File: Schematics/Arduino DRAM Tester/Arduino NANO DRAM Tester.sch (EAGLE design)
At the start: 53 parts, among them IC1 4164/41256, IC2 4116, Q1 2N3906

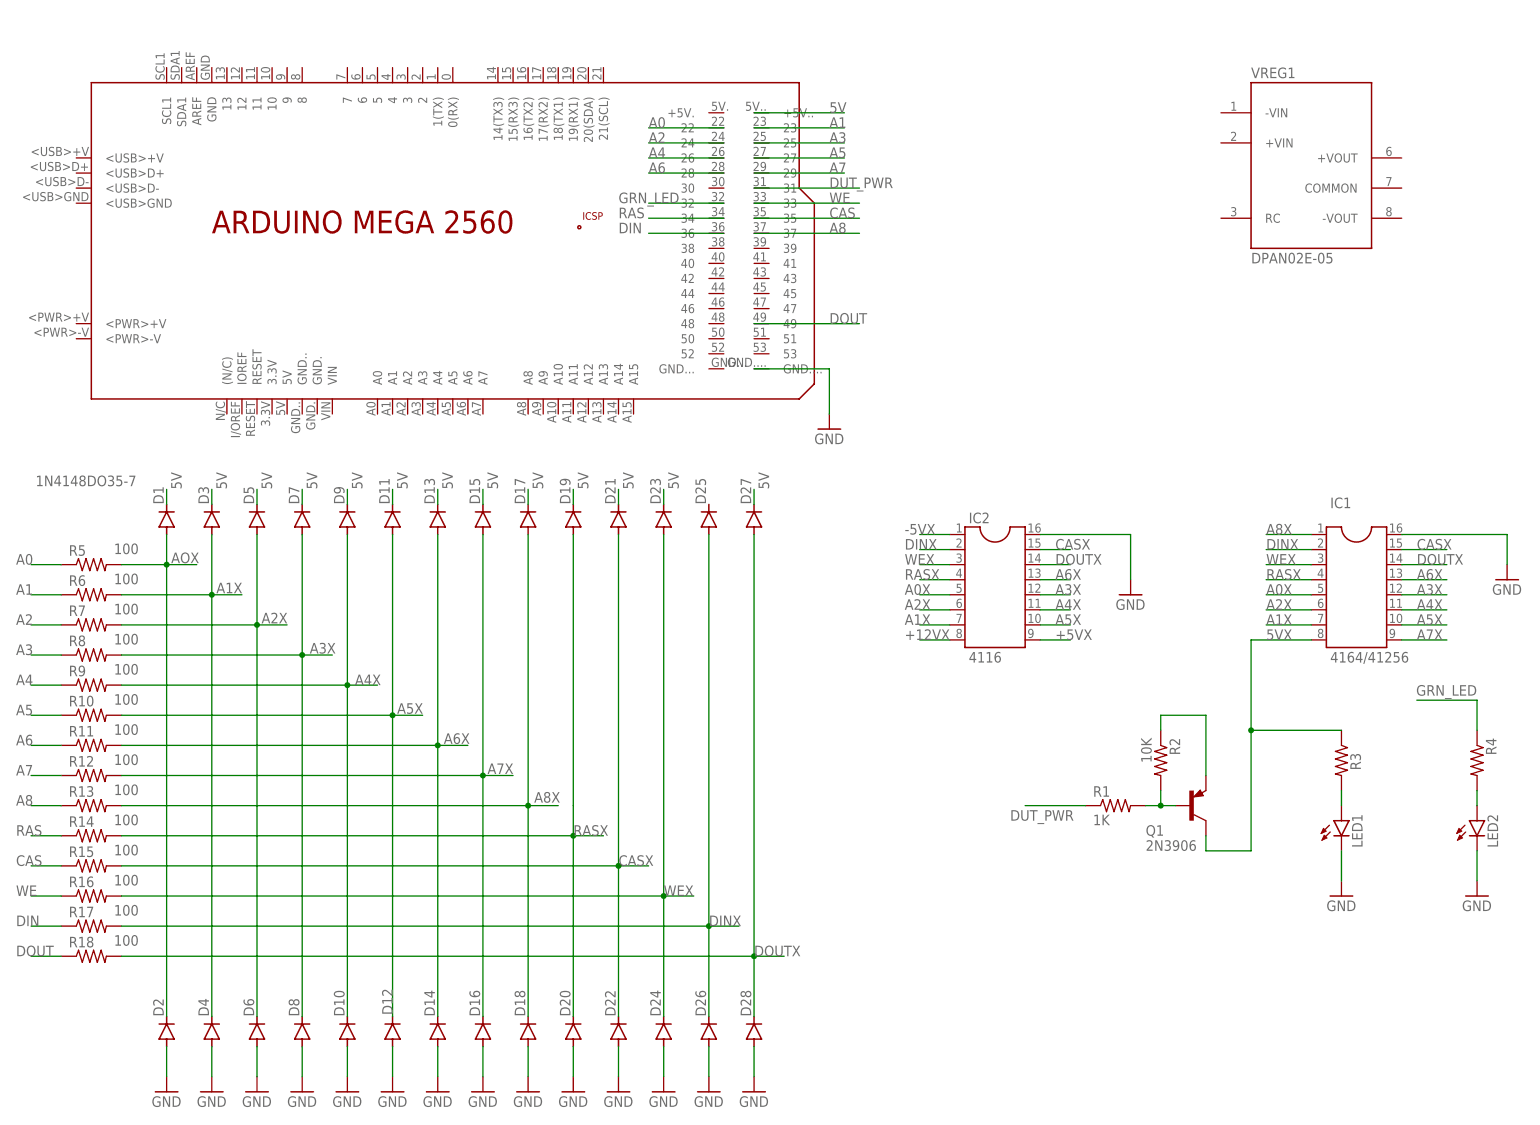
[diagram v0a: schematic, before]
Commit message: Added  def for Nano and Micro. Tested on Mega and Micro. Will add display next
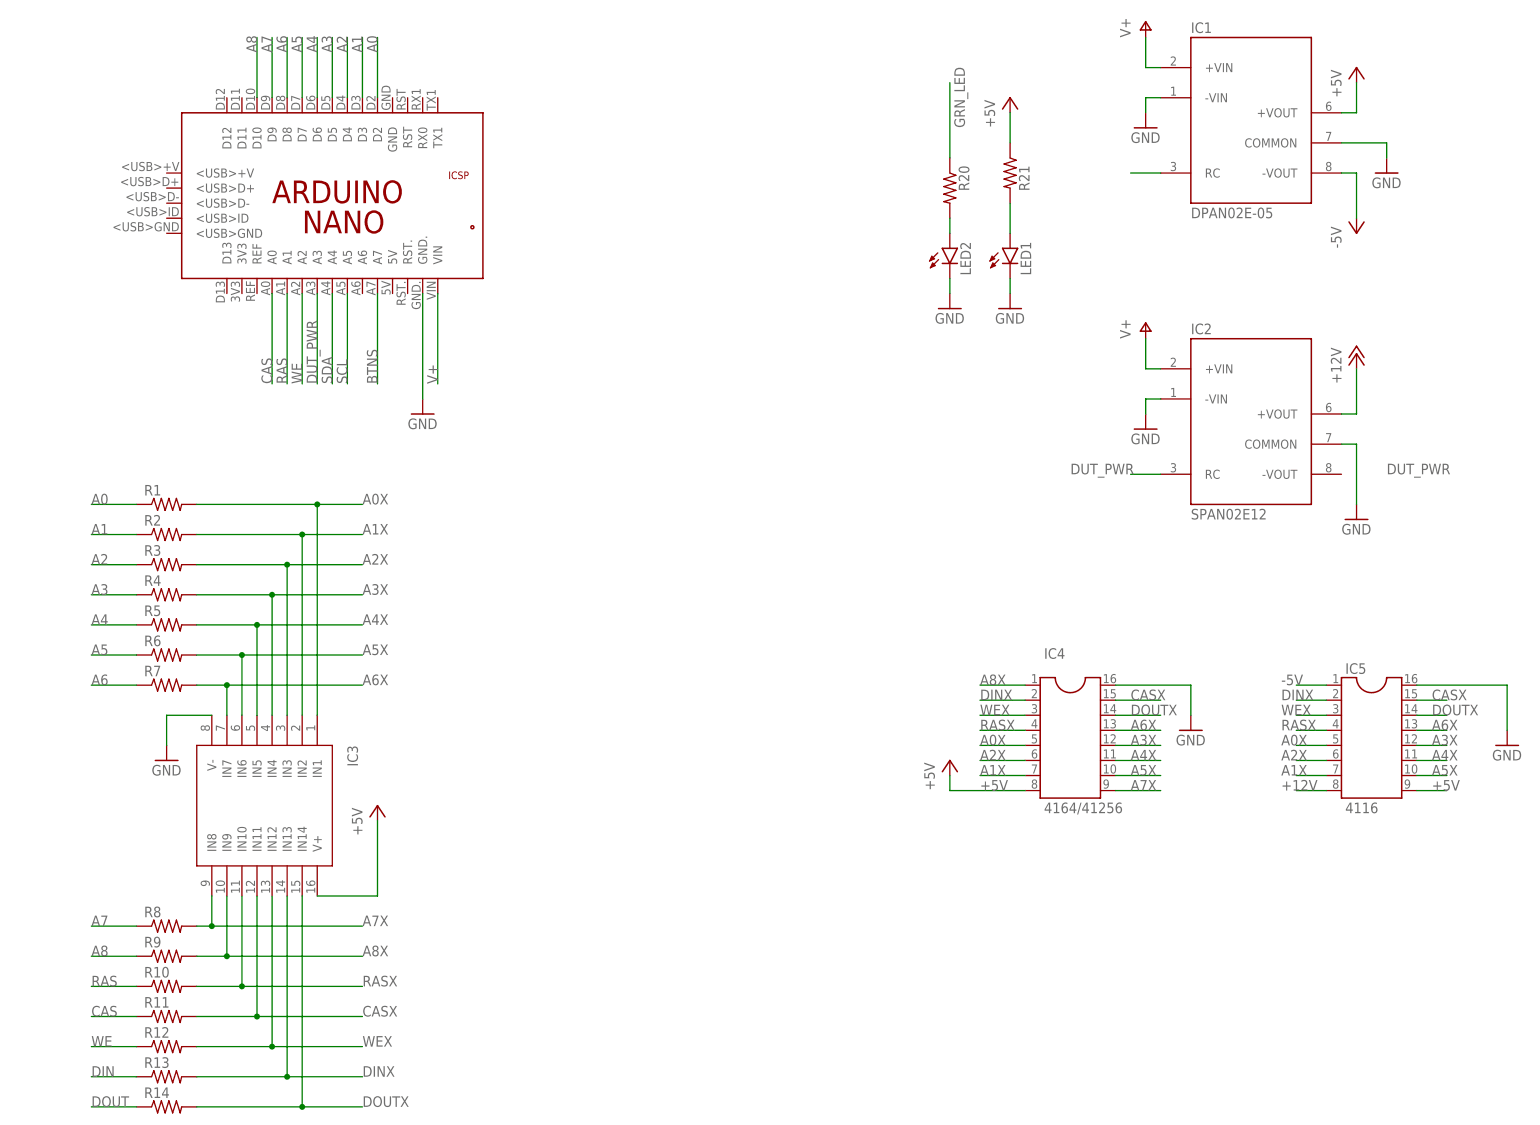
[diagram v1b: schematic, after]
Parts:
- removed D1, D10, D11, D12, D13, D14, D15, D16, D17, D18, D19, D2, D20, D21, D22, D23, D24, D25, D26, D27, D28, D3, D4, D5, D6, D7, D8, D9: 1N4148DO35-7, diode:1N4148DO35-7
- removed Q1: 2N3906, transistor-pnp:2N3906
- removed R15, R16, R17, R18: 100, resistor:R-US_0309/10
- removed VREG1: DPAN02E-05, MW DPAN02:DPAN02
- added IC3: (no value), Littlefuse:SP720
- added IC4: 4164/41256, ic-package:DIL16
- added IC5: 4116, ic-package:DIL16S
- added R20, R21: (no value), resistor:R-US_0309/10
- IC1: value 4164/41256 -> DPAN02E-05; device ic-package:DIL16 -> MW DPAN02:DPAN02
- IC2: value 4116 -> SPAN02E12; device ic-package:DIL16S -> MW DPAN02:DPAN02
- PCB1: value ARDUINO_MEGA2560 -> ARDUINO_NANO; device E14_Arduino_revC:ARDUINO_MEGA2560 -> E14_Arduino_revC:ARDUINO_NANO
- R1: value 1K -> (none); device resistor:R-US_0309/10 -> rcl:R-US_V235/17
- R10, R11, R12, R13, R14, R5, R6, R7, R8, R9: value 100 -> (none); device resistor:R-US_0309/10 -> rcl:R-US_V235/17
- R2: value 10K -> (none); device resistor:R-US_0309/10 -> rcl:R-US_V235/17
- R3, R4: device resistor:R-US_0309/10 -> rcl:R-US_V235/17
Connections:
- removed net +12VX: IC2.8
- removed net +5VX: IC2.9
- removed net -5VX: IC2.1
- removed net 5V: D1.C, D11.C, D13.C, D15.C, D17.C, D19.C, D21.C, D23.C, D27.C, D3.C, D5.C, D7.C, D9.C, PCB1.+5V..
- removed net 5VX: IC1.8, Q1.C, R3.1
- removed net A8X1: D19.A
- removed net AOX: D1.A, D2.C, R5.2
- removed net N$17: Q1.E, R2.1
- removed net N$7: Q1.B, R1.2, R2.2
- new net +12V: IC2.+VOUT, IC5.8
- new net +5V: IC1.+VOUT, IC3.V+, IC4.8, IC5.9, R21.1
- new net -5V: IC1.-VOUT, IC5.1
- new net BTNS: PCB1.A7
- new net SCL: PCB1.A5
- new net SDA: PCB1.A4
- new net V+: IC1.+VIN, IC2.+VIN, PCB1.VIN
- net A0: now also PCB1.D2, R1.1; no longer PCB1.22, R5.1
- net A0X: now also IC3.IN1, IC4.5, IC5.5, R1.2; no longer IC1.5, IC2.5
- net A1: now also PCB1.D3, R2.1; no longer PCB1.23, R6.1
- net A1X: now also IC3.IN2, IC4.7, IC5.7, R2.2; no longer D3.A, D4.C, IC1.7, IC2.7, R6.2
- net A2: now also PCB1.D4, R3.1; no longer PCB1.24, R7.1
- net A2X: now also IC3.IN3, IC4.6, IC5.6, R3.2; no longer D5.A, D6.C, IC1.6, IC2.6, R7.2
- net A3: now also PCB1.D5, R4.1; no longer PCB1.25, R8.1
- net A3X: now also IC3.IN4, IC4.12, IC5.12, R4.2; no longer D7.A, D8.C, IC1.12, IC2.12, R8.2
- net A4: now also PCB1.D6, R5.1; no longer PCB1.26, R9.1
- net A4X: now also IC3.IN5, IC4.11, IC5.11, R5.2; no longer D10.C, D9.A, IC1.11, IC2.11, R9.2
- net A5: now also PCB1.D7, R6.1; no longer PCB1.27, R10.1
- net A5X: now also IC3.IN6, IC4.10, IC5.10, R6.2; no longer D11.A, D12.C, IC1.10, IC2.10, R10.2
- net A6: now also PCB1.D8, R7.1; no longer PCB1.28, R11.1
- net A6X: now also IC3.IN7, IC4.13, IC5.13, R7.2; no longer D13.A, D14.C, IC1.13, IC2.13, R11.2
- net A7: now also PCB1.D9, R8.1; no longer PCB1.29, R12.1
- net A7X: now also IC3.IN8, IC4.9, R8.2; no longer D15.A, D16.C, IC1.9, R12.2
- net A8: now also PCB1.D10, R9.1; no longer PCB1.37, R13.1
- net A8X: now also IC3.IN9, IC4.1, R9.2; no longer D17.A, D18.C, IC1.1, R13.2
- net CAS: now also PCB1.A0, R11.1; no longer PCB1.35, R15.1
- net CASX: now also IC3.IN11, IC4.15, IC5.15, R11.2; no longer D21.A, D22.C, IC1.15, IC2.15, R15.2
- net DIN: now also R13.1; no longer PCB1.36, R17.1
- net DINX: now also IC3.IN13, IC4.2, IC5.2, R13.2; no longer D25.A, D26.C, IC1.2, IC2.2, R17.2
- net DOUT: now also R14.1; no longer PCB1.49, R18.1
- net DOUTX: now also IC3.IN14, IC4.14, IC5.14, R14.2; no longer D27.A, D28.C, IC1.14, IC2.14, R18.2
- net DUT_PWR: now also IC1.RC, IC2.RC, PCB1.A3; no longer PCB1.31, R1.1
- net GND: now also IC1.-VIN, IC1.COMMON, IC2.-VIN, IC2.COMMON, IC3.V-, IC4.16, IC5.16, PCB1.GND.; no longer D10.A, D12.A, D14.A, D16.A, D18.A, D2.A, D20.A, D22.A, D24.A, D26.A, D28.A, D4.A, D6.A, D8.A, IC1.16, IC2.16, PCB1.GND....
- net GRN_LED: now also R20.1; no longer PCB1.32, R4.1
- net N$20: now also R20.2; no longer R4.2
- net N$6: now also R21.2; no longer R3.2
- net RAS: now also PCB1.A1, R10.1; no longer PCB1.34, R14.1
- net RASX: now also IC3.IN10, IC4.4, IC5.4, R10.2; no longer D20.C, IC1.4, IC2.4, R14.2
- net WE: now also PCB1.A2, R12.1; no longer PCB1.33, R16.1
- net WEX: now also IC3.IN12, IC4.3, IC5.3, R12.2; no longer D23.A, D24.C, IC1.3, IC2.3, R16.2
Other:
- moved on the sheet: LED1, LED2, R1, R10, R11, R12, R13, R14, R2, R3, R4, R5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
